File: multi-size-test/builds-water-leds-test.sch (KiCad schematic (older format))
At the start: 20 parts, among them P1 CONN_2, P2 CONN_2, P3 CONN_2, P4 CONN_2

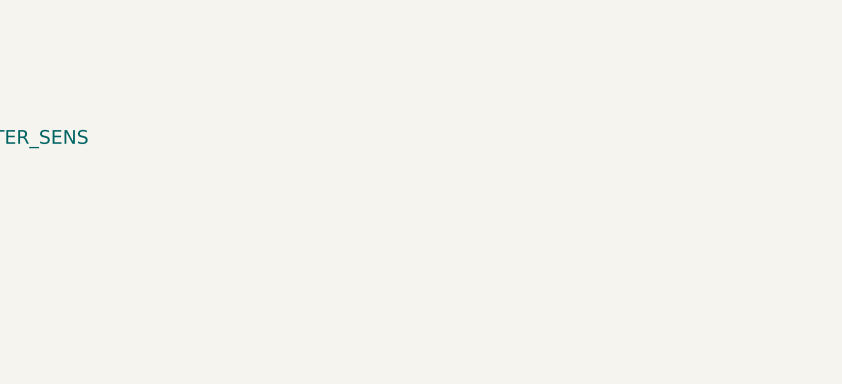
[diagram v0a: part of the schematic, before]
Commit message: Added some more credits to Antonin Fourneau
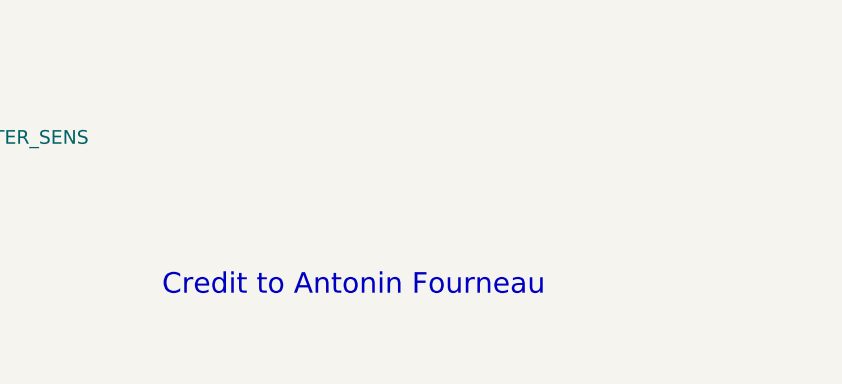
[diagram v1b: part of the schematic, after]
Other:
- note added: "Credit to Antonin Fourneau"
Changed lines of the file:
@@
-EESchema Schematic File Version 2  date Wed 22 Aug 2012 10:36:07 AM EDT
+EESchema Schematic File Version 2  date Fri 24 Aug 2012 04:59:22 PM EDT
 LIBS:power
 LIBS:device
@@
 Sheet 1 1
 Title "Water LED Graffiti Test"
-Date "22 aug 2012"
+Date "24 aug 2012"
 Rev "A"
 Comp "Christopher Woodall - BUILDS (builds.cc)"
@@
 Text Notes 7100 2250 0    100  ~ 0
 Power Connectors (Left, Right, Top Bottom)
+Text Notes 6350 7250 0    90   ~ 0
+Credit to Antonin Fourneau
 $EndSCHEMATC
